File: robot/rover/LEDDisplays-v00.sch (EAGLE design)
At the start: 19 parts, among them U1 TLC5940PWP, U2 TLC5940PWP, U3 TLC5940PWP

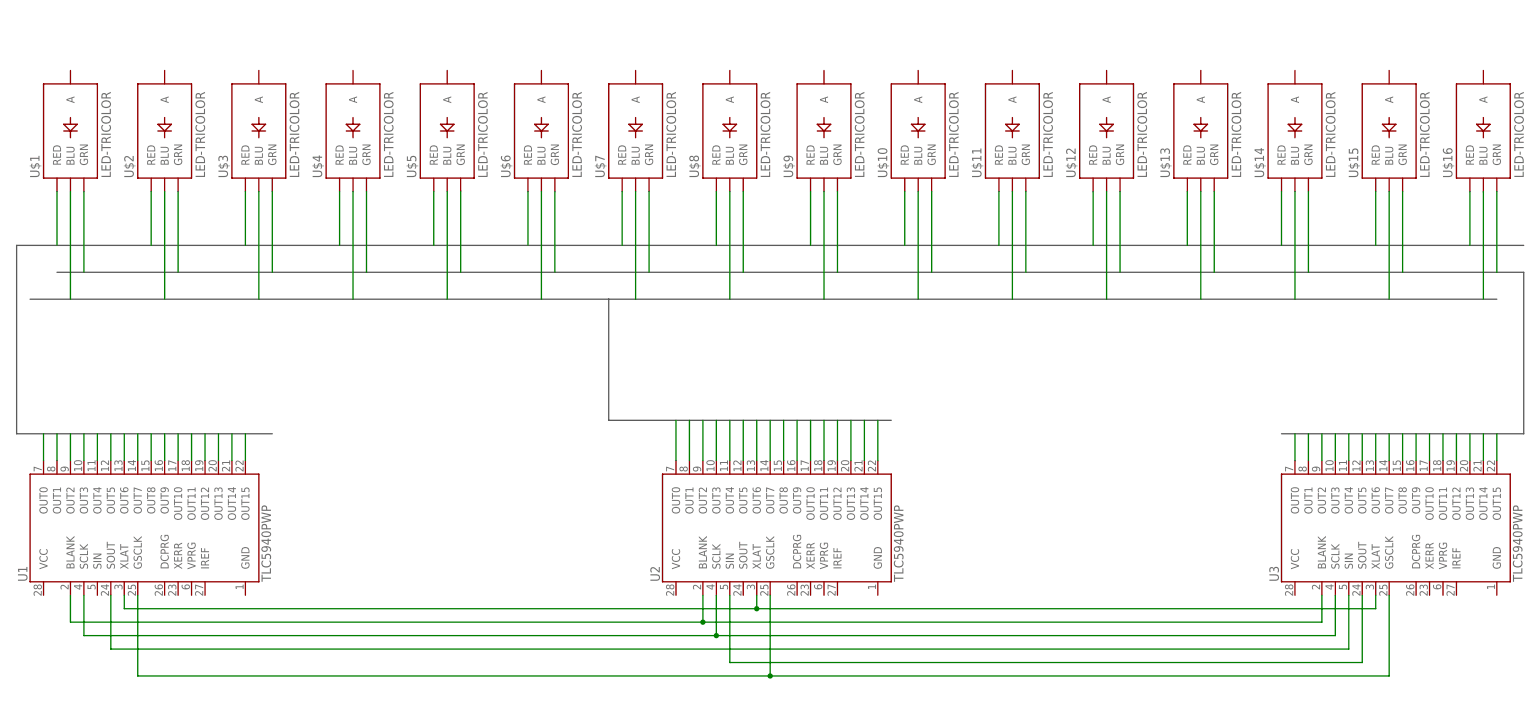
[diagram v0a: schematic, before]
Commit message: Adding connections to RGB
Signed-off-by: J.C. Woltz <jc.woltz@ludowici.com>
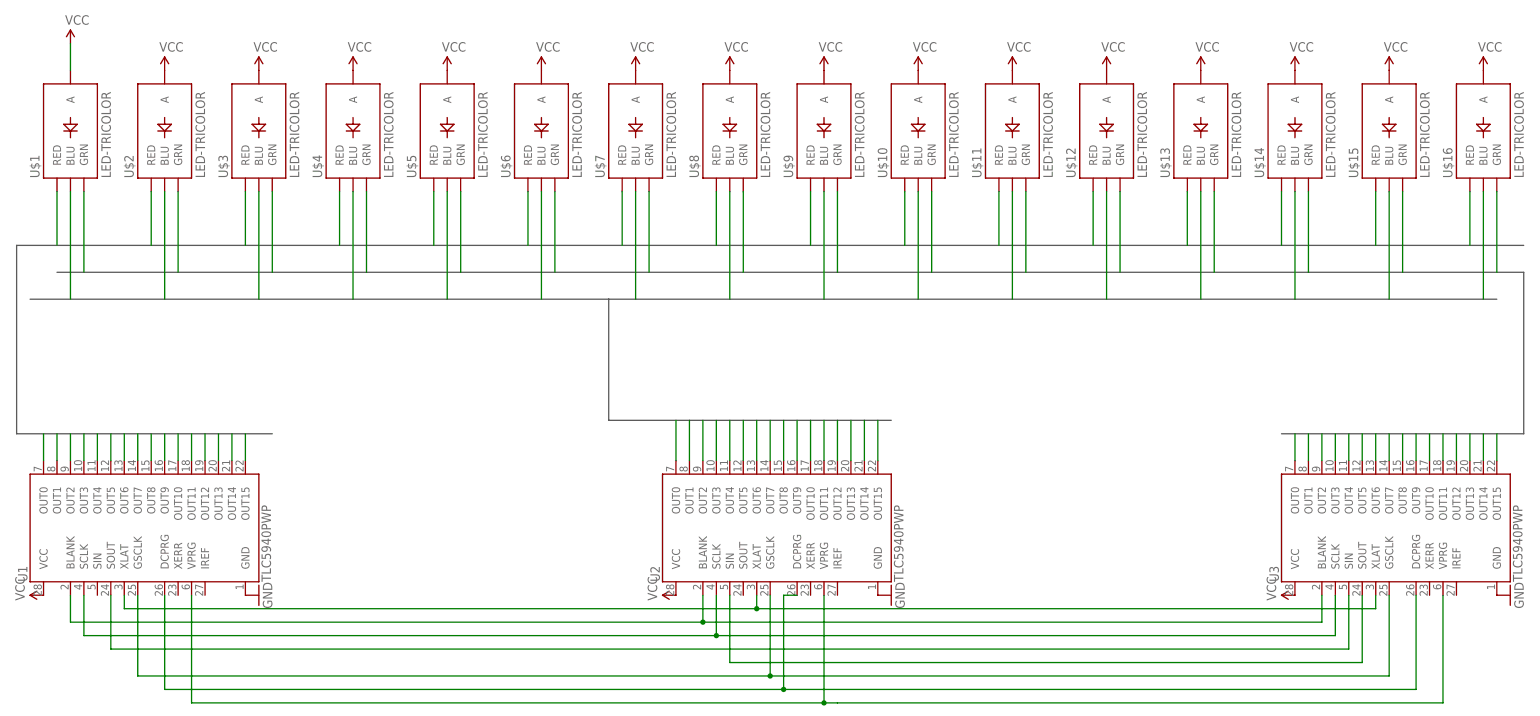
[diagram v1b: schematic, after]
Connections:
- net N$3 renamed SCLK
- net N$4 renamed BLANK
- net N$5 renamed XLAT
- net N$6 renamed GSCLK
- new net DCPRG: U1.DCPRG, U2.DCPRG, U3.DCPRG
- new net GND: U1.GND, U2.GND, U3.GND
- new net VCC: U$1.A, U$10.A, U$11.A, U$12.A, U$13.A, U$14.A, U$15.A, U$16.A, U$2.A, U$3.A, U$4.A, U$5.A, U$6.A, U$7.A, U$8.A, U$9.A, U1.VCC, U2.VCC, U3.VCC
- new net VPRG: U1.VPRG, U2.VPRG, U3.VPRG
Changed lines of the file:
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@@
 </variantdefs>
 <classes>
-<class number="0" name="default" width="0" drill="0">
+<class number="0" name="default" width="0.1524" drill="0">
+</class>
+<class number="1" name="VCC" width="0.254" drill="0">
 </class>
 </classes>
@@
 <part name="U$15" library="SparkFun-LED" deviceset="LED-TRICOLOR" device=""/>
 <part name="U$16" library="SparkFun-LED" deviceset="LED-TRICOLOR" device=""/>
+<part name="GND1" library="SparkFun-Aesthetics" deviceset="GND" device=""/>
+<part name="GND2" library="SparkFun-Aesthetics" deviceset="GND" device=""/>
+<part name="GND3" library="SparkFun-Aesthetics" deviceset="GND" device=""/>
+<part name="SUPPLY1" library="SparkFun-Aesthetics" deviceset="VCC" device=""/>
+<part name="SUPPLY2" library="SparkFun-Aesthetics" deviceset="VCC" device=""/>
+<part name="SUPPLY3" library="SparkFun-Aesthetics" deviceset="VCC" device=""/>
+<part name="SUPPLY4" library="SparkFun-Aesthetics" deviceset="VCC" device=""/>
+<part name="SUPPLY5" library="SparkFun-Aesthetics" deviceset="VCC" device=""/>
+<part name="SUPPLY6" library="SparkFun-Aesthetics" deviceset="VCC" device=""/>
+<part name="SUPPLY7" library="SparkFun-Aesthetics" deviceset="VCC" device=""/>
+<part name="SUPPLY8" library="SparkFun-Aesthetics" deviceset="VCC" device=""/>
+<part name="SUPPLY9" library="SparkFun-Aesthetics" deviceset="VCC" device=""/>
+<part name="SUPPLY10" library="SparkFun-Aesthetics" deviceset="VCC" device=""/>
+<part name="SUPPLY11" library="SparkFun-Aesthetics" deviceset="VCC" device=""/>
+<part name="SUPPLY12" library="SparkFun-Aesthetics" deviceset="VCC" device=""/>
+<part name="SUPPLY13" library="SparkFun-Aesthetics" deviceset="VCC" device=""/>
+<part name="SUPPLY14" library="SparkFun-Aesthetics" deviceset="VCC" device=""/>
+<part name="SUPPLY15" library="SparkFun-Aesthetics" deviceset="VCC" device=""/>
+<part name="SUPPLY16" library="SparkFun-Aesthetics" deviceset="VCC" device=""/>
+<part name="SUPPLY17" library="SparkFun-Aesthetics" deviceset="VCC" device=""/>
+<part name="SUPPLY18" library="SparkFun-Aesthetics" deviceset="VCC" device=""/>
+<part name="SUPPLY19" library="SparkFun-Aesthetics" deviceset="VCC" device=""/>
 </parts>
 <sheets>
@@
 <instance part="U$15" gate="G$1" x="261.62" y="76.2" rot="R90"/>
 <instance part="U$16" gate="G$1" x="279.4" y="76.2" rot="R90"/>
+<instance part="GND1" gate="1" x="170.18" y="-10.16" rot="R90"/>
+<instance part="GND2" gate="1" x="287.02" y="-10.16" rot="R90"/>
+<instance part="GND3" gate="1" x="50.8" y="-10.16" rot="R90"/>
+<instance part="SUPPLY1" gate="1" x="10.16" y="-10.16" rot="R90"/>
+<instance part="SUPPLY2" gate="1" x="129.54" y="-10.16" rot="R90"/>
+<instance part="SUPPLY3" gate="1" x="246.38" y="-10.16" rot="R90"/>
+<instance part="SUPPLY4" gate="1" x="15.24" y="93.98"/>
+<instance part="SUPPLY5" gate="1" x="33.02" y="88.9"/>
+<instance part="SUPPLY6" gate="1" x="50.8" y="88.9"/>
+<instance part="SUPPLY7" gate="1" x="68.58" y="88.9"/>
+<instance part="SUPPLY8" gate="1" x="86.36" y="88.9"/>
+<instance part="SUPPLY9" gate="1" x="104.14" y="88.9"/>
+<instance part="SUPPLY10" gate="1" x="121.92" y="88.9"/>
+<instance part="SUPPLY11" gate="1" x="139.7" y="88.9"/>
+<instance part="SUPPLY12" gate="1" x="157.48" y="88.9"/>
+<instance part="SUPPLY13" gate="1" x="175.26" y="88.9"/>
+<instance part="SUPPLY14" gate="1" x="193.04" y="88.9"/>
+<instance part="SUPPLY15" gate="1" x="210.82" y="88.9"/>
+<instance part="SUPPLY16" gate="1" x="228.6" y="88.9"/>
+<instance part="SUPPLY17" gate="1" x="246.38" y="88.9"/>
+<instance part="SUPPLY18" gate="1" x="264.16" y="88.9"/>
+<instance part="SUPPLY19" gate="1" x="281.94" y="88.9"/>
 </instances>
 <busses>
@@
 </segment>
 </net>
-<net name="N$3" class="0">
+<net name="SCLK" class="0">
 <segment>
 <pinref part="U3" gate="G$1" pin="SCLK"/>
@@
 </segment>
 </net>
-<net name="N$4" class="0">
+<net name="BLANK" class="0">
 <segment>
 <pinref part="U1" gate="G$1" pin="BLANK"/>
@@
 </segment>
 </net>
-<net name="N$5" class="0">
+<net name="XLAT" class="0">
 <segment>
 <pinref part="U3" gate="G$1" pin="XLAT"/>
@@
 </segment>
 </net>
-<net name="N$6" class="0">
+<net name="GSCLK" class="0">
 <segment>
 <pinref part="U2" gate="G$1" pin="GSCLK"/>
@@
 </segment>
 </net>
+<net name="DCPRG" class="0">
+<segment>
+<pinref part="U3" gate="G$1" pin="DCPRG"/>
+<wire x1="269.24" y1="-10.16" x2="269.24" y2="-27.94" width="0.1524" layer="91"/>
+<wire x1="269.24" y1="-27.94" x2="149.86" y2="-27.94" width="0.1524" layer="91"/>
+<pinref part="U2" gate="G$1" pin="DCPRG"/>
+<wire x1="149.86" y1="-27.94" x2="149.86" y2="-10.16" width="0.1524" layer="91"/>
+<wire x1="149.86" y1="-10.16" x2="152.4" y2="-10.16" width="0.1524" layer="91"/>
+<pinref part="U1" gate="G$1" pin="DCPRG"/>
+<wire x1="33.02" y1="-10.16" x2="33.02" y2="-27.94" width="0.1524" layer="91"/>
+<wire x1="33.02" y1="-27.94" x2="149.86" y2="-27.94" width="0.1524" layer="91"/>
+<junction x="149.86" y="-27.94"/>
+</segment>
+</net>
+<net name="VPRG" class="0">
+<segment>
+<pinref part="U1" gate="G$1" pin="VPRG"/>
+<wire x1="38.1" y1="-10.16" x2="38.1" y2="-30.48" width="0.1524" layer="91"/>
+<wire x1="38.1" y1="-30.48" x2="157.48" y2="-30.48" width="0.1524" layer="91"/>
+<pinref part="U2" gate="G$1" pin="VPRG"/>
+<wire x1="160.02" y1="-30.48" x2="157.48" y2="-30.48" width="0.1524" layer="91"/>
+<wire x1="157.48" y1="-30.48" x2="157.48" y2="-10.16" width="0.1524" layer="91"/>
+<pinref part="U3" gate="G$1" pin="VPRG"/>
+<wire x1="274.32" y1="-10.16" x2="274.32" y2="-30.48" width="0.1524" layer="91"/>
+<wire x1="274.32" y1="-30.48" x2="160.02" y2="-30.48" width="0.1524" layer="91"/>
+<junction x="157.48" y="-30.48"/>
+</segment>
+</net>
+<net name="GND" class="0">
+<segment>
+<pinref part="U2" gate="G$1" pin="GND"/>
+<pinref part="GND1" gate="1" pin="GND"/>
+</segment>
+<segment>
+<pinref part="U3" gate="G$1" pin="GND"/>
+<pinref part="GND2" gate="1" pin="GND"/>
+</segment>
+<segment>
+<pinref part="U1" gate="G$1" pin="GND"/>
+<pinref part="GND3" gate="1" pin="GND"/>
+</segment>
+</net>
+<net name="VCC" class="1">
+<segment>
+<pinref part="U1" gate="G$1" pin="VCC"/>
+<pinref part="SUPPLY1" gate="1" pin="VCC"/>
+</segment>
+<segment>
+<pinref part="U2" gate="G$1" pin="VCC"/>
+<pinref part="SUPPLY2" gate="1" pin="VCC"/>
+</segment>
+<segment>
+<pinref part="U3" gate="G$1" pin="VCC"/>
+<pinref part="SUPPLY3" gate="1" pin="VCC"/>
+</segment>
+<segment>
+<pinref part="U$1" gate="G$1" pin="A"/>
+<pinref part="SUPPLY4" gate="1" pin="VCC"/>
+<wire x1="15.24" y1="93.98" x2="15.24" y2="88.9" width="0.1524" layer="91"/>
+</segment>
+<segment>
+<pinref part="U$2" gate="G$1" pin="A"/>
+<pinref part="SUPPLY5" gate="1" pin="VCC"/>
+</segment>
+<segment>
+<pinref part="U$3" gate="G$1" pin="A"/>
+<pinref part="SUPPLY6" gate="1" pin="VCC"/>
+</segment>
+<segment>
+<pinref part="U$4" gate="G$1" pin="A"/>
+<pinref part="SUPPLY7" gate="1" pin="VCC"/>
+</segment>
+<segment>
+<pinref part="U$5" gate="G$1" pin="A"/>
+<pinref part="SUPPLY8" gate="1" pin="VCC"/>
+</segment>
+<segment>
+<pinref part="U$6" gate="G$1" pin="A"/>
+<pinref part="SUPPLY9" gate="1" pin="VCC"/>
+</segment>
+<segment>
+<pinref part="U$7" gate="G$1" pin="A"/>
+<pinref part="SUPPLY10" gate="1" pin="VCC"/>
+</segment>
+<segment>
+<pinref part="U$8" gate="G$1" pin="A"/>
+<pinref part="SUPPLY11" gate="1" pin="VCC"/>
+</segment>
+<segment>
+<pinref part="U$9" gate="G$1" pin="A"/>
+<pinref part="SUPPLY12" gate="1" pin="VCC"/>
+</segment>
+<segment>
+<pinref part="U$10" gate="G$1" pin="A"/>
+<pinref part="SUPPLY13" gate="1" pin="VCC"/>
+</segment>
+<segment>
+<pinref part="U$11" gate="G$1" pin="A"/>
+<pinref part="SUPPLY14" gate="1" pin="VCC"/>
+</segment>
+<segment>
+<pinref part="U$12" gate="G$1" pin="A"/>
+<pinref part="SUPPLY15" gate="1" pin="VCC"/>
+</segment>
+<segment>
+<pinref part="U$13" gate="G$1" pin="A"/>
+<pinref part="SUPPLY16" gate="1" pin="VCC"/>
+</segment>
+<segment>
+<pinref part="U$14" gate="G$1" pin="A"/>
+<pinref part="SUPPLY17" gate="1" pin="VCC"/>
+</segment>
+<segment>
+<pinref part="U$15" gate="G$1" pin="A"/>
+<pinref part="SUPPLY18" gate="1" pin="VCC"/>
+</segment>
+<segment>
+<pinref part="U$16" gate="G$1" pin="A"/>
+<pinref part="SUPPLY19" gate="1" pin="VCC"/>
+</segment>
+</net>
